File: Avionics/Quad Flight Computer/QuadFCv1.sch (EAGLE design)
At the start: 122 parts, among them J2 1050270001, Q1 DMP2035U, Q2 DMP2035U, Q3 DMP2035U, SW1 PTS635VL31-VERT, U1 TM4C123GH6PZ, U10 LTC4412, U11 AP7215-33YG-13, U2 74LVC4245APW, U3 ATMEGA32U2-MU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

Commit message: Added some connectors
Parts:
- added JP1, JP2: M101X10-SMT-0.05, QuadFCv1:M101X10-SMT-0.05
- added JP3, JP4: M12, QuadFCv1:M12
- added R57: 0, QuadFCv1:RESISTOR0402-RES
- added R58, R59: 10K, QuadFCv1:RESISTOR0402-RES
- added U4: MCP6L91T-E/OT, QuadFCv1:MCP6L91T-E/OT
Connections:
- removed net EXT_I2C_SCL: I2C.3
- removed net EXT_I2C_SDA: I2C.2
- removed net FC_AIN0: U1PORTE.PE3/AIN0
- removed net FC_AIN1: U1PORTE.PE2/AIN1
- removed net FC_AIN20: U1PORTE.PE7/AIN20/CAN1TX/U1RI
- removed net FC_AIN21: U1PORTE.PE6/AIN21/CAN1RX
- removed net FC_AIN4: U1PORTD.PD7/AIN4/M0FAULT1/NMI/PHB0/U2TX/WT5CCP1
- removed net FC_AIN5: U1PORTD.PD6/AIN5/M0FAULT0/PHA0/U2RX/WT5CCP0
- removed net FC_PA6: U1PORTA.PA6/I2C1SCL/M1PWM2
- removed net FC_PA7: U1PORTA.PA7/I2C1SDA/M1PWM3
- removed net FC_PD5: U1PORTD.PD5/AIN6/U6TX/WT4CCP1
- removed net FC_PF4: U1PORTF.PF4/IDX0/M0FAULT2/M1FAULT0/T2CCP0/TRD3/U1DTR/USB0EPEN
- removed net FC_PF5: U1PORTF.PF5/M0FAULT3/T2CCP1/USB0PFLT
- removed net FC_PF6: U1PORTF.PF6/I2C2SCL/T3CCP0
- removed net FC_PF7: U1PORTF.PF7/I2C2SDA/M1FAULT0/T3CCP1
- removed net FC_PJ2: U1PORTJ.PJ2/IDX0/T2CCP0/U5RX
- removed net FC_U0RX: U1PORTA.PA0/CAN1RX/U0RX
- removed net FC_U0TX: U1PORTA.PA1/CAN1TX/U0TX
- removed net FC_U1RX: U1PORTC.PC4/C1-/IDX1/M0PWM6/U1RTS/U1RX/U4RX/WT0CCP0
- removed net FC_U1TX: U1PORTC.PC5/C1+/M0PWM7/PHA1/U1CTS/U1TX/U4TX/WT0CCP1
- removed net FC_U3RX: U1PORTC.PC6/C0+/PHB1/U3RX/USB0EPEN/WT1CCP0
- removed net FC_U3TX: U1PORTC.PC7/C0-/U3TX/USB0PFLT/WT1CCP1
- removed net FC_U7RX: U1PORTE.PE0/AIN3/U7RX
- removed net FC_U7TX: U1PORTE.PE1/AIN2/U7TX
- removed net FC_USB0VBUS: U1PORTB.PB1/T2CCP1/U1TX/USB0VBUS
- removed net PPM_VBUS: U3.UVCC
- removed net RADIO_UART_RX: RADIO1.3
- removed net RADIO_UART_TX: RADIO1.2
- new net BUZZER_PWM: U1PORTA.PA7/I2C1SDA/M1PWM3, U4.+IN
- new net N$40: R57.1, U4.OUT
- new net N$43: R58.1, R59.2, U4.-IN
- new net RADIO_RX: RADIO1.3, U1PORTE.PE0/AIN3/U7RX
- new net RADIO_TX: RADIO1.2, U1PORTE.PE1/AIN2/U7TX
- new net VUSB_F: F1.1, Q1.D, Q3.S, U1PORTB.PB1/T2CCP1/U1TX/USB0VBUS, U3.UVCC
- net 3.3V: now also R58.2
- net 5V: now also U4.V+
- net FC_IMU_INT: now also U1PORTF.PF7/I2C2SDA/M1FAULT0/T3CCP1
- net FC_MAG_DRDY_L: now also U1PORTA.PA6/I2C1SCL/M1PWM2
- net FC_MEM_SEL: now also U1PORTJ.PJ2/IDX0/T2CCP0/U5RX
- net FC_PPM_IN: now also U1PORTC.PC7/C0-/U3TX/USB0PFLT/WT1CCP1
- net FC_PPM_STATUS0: now also U1PORTF.PF6/I2C2SCL/T3CCP0
- net FC_PPM_STATUS1: now also U1PORTF.PF5/M0FAULT3/T2CCP1/USB0PFLT
- net FC_SD_PRESENT: now also U1PORTD.PD5/AIN6/U6TX/WT4CCP1
- net FC_SENSE_SCL: now also I2C.3
- net FC_SENSE_SDA: now also I2C.2
- net FC_USB_STATUS: now also U1PORTF.PF4/IDX0/M0FAULT2/M1FAULT0/T2CCP0/TRD3/U1DTR/USB0EPEN
- net GND: now also BZR.2, R59.1, U4.V-
- net GPS_RX: now also U1PORTC.PC4/C1-/IDX1/M0PWM6/U1RTS/U1RX/U4RX/WT0CCP0
- net GPS_TX: now also U1PORTC.PC5/C1+/M0PWM7/PHA1/U1CTS/U1TX/U4TX/WT0CCP1
- net ISENSE1: now also U1PORTE.PE7/AIN20/CAN1TX/U1RI
- net ISENSE2: now also U1PORTE.PE6/AIN21/CAN1RX
- net ISENSE3: now also U1PORTE.PE3/AIN0
- net ISENSE4: now also U1PORTD.PD7/AIN4/M0FAULT1/NMI/PHB0/U2TX/WT5CCP1
- net ISENSE5V: now also U1PORTD.PD6/AIN5/M0FAULT0/PHA0/U2RX/WT5CCP0
- net N$42: now also BZR.1, R57.2; no longer F1.1, Q1.D, Q3.S
- net PPM_RX: now also U1PORTA.PA0/CAN1RX/U0RX
- net PPM_TX: now also U1PORTA.PA1/CAN1TX/U0TX
- net USB_EPEN: now also U1PORTC.PC6/C0+/PHB1/U3RX/USB0EPEN/WT1CCP0
- net VBATTSENSE: now also U1PORTE.PE2/AIN1

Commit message: Finished pinout for shield headers
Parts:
- added R60: 100k, QuadFCv1:RESISTOR0402-RES
- JP2: value M101X10-SMT-0.05 -> M12; device QuadFCv1:M101X10-SMT-0.05 -> QuadFCv1:M12
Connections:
- net 3.3V: now also JP3.2
- net 5V: now also JP3.1
- net 5VBATT: now also R60.2
- net BUZZER_PWM: now also JP1.5
- net FC_IMU_MISO: now also JP2.2
- net FC_IMU_MOSI: now also JP2.3
- net FC_IMU_SCLK: now also JP2.1
- net FC_JTAG_TCK: now also JP4.5
- net FC_JTAG_TDI: now also JP4.7
- net FC_JTAG_TDO: now also JP4.8
- net FC_JTAG_TMS: now also JP4.6
- net FC_MEM_CLK: now also JP3.4
- net FC_MEM_MISO: now also JP3.5
- net FC_MEM_MOSI: now also JP3.3
- net FC_PB2: now also JP4.12
- net FC_PB3: now also JP4.11
- net FC_PB4: now also JP4.1
- net FC_PB5: now also JP4.2
- net FC_PD0: now also JP3.9
- net FC_PD1: now also JP3.8
- net FC_PD2: now also JP3.7
- net FC_PD3: now also JP3.6
- net FC_PD4: now also JP3.10
- net FC_PE4: now also JP3.12
- net FC_PE5: now also JP3.11
- net FC_PF0: now also JP2.4
- net FC_PF1: now also JP2.5
- net FC_PF2: now also JP2.6
- net FC_PF3: now also JP2.7
- net FC_PG2: now also JP2.10
- net FC_PG3: now also JP2.9
- net FC_PG4: now also JP4.10
- net FC_PG5: now also JP4.9
- net FC_PG6: now also JP4.4
- net FC_PG7: now also JP4.3
- net FC_RESET_L: now also JP2.8
- net FC_SENSE_SCL: now also JP2.11
- net FC_SENSE_SDA: now also JP2.12
- net GND: now also JP1.1, JP1.2
- net GPS_RX: now also JP1.6
- net GPS_TX: now also JP1.7
- net PPM_RX: now also JP1.8
- net PPM_TX: now also JP1.9
- net RADIO_RX: now also JP1.3
- net RADIO_TX: now also JP1.4
- net USB_EPEN: now also R60.1
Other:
- moved on the sheet: JP1, JP3, JP4

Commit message: Lots more routing done
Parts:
- removed R3, R5: 22-DNP, QuadFCv1:RESISTOR0402-RES
- removed R36: 1k, QuadFCv1:RESISTOR0402-RES
- removed R8, R9: DNP, QuadFCv1:RESISTOR0603-RES
- C12, C9: value 1uF -> 1.8uF
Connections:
- removed net FC_USB_STATUS: R36.1, U1PORTF.PF4/IDX0/M0FAULT2/M1FAULT0/T2CCP0/TRD3/U1DTR/USB0EPEN
- removed net N$28: R3.2, R7.2, U12.D-
- removed net PPM_USBDM: R3.1, U3.D-
- removed net PPM_USBDP: R5.1, U3.D+
- removed net PPM_USB_STATUS: R36.2, U3.(AIN2/PCINT11)PC2
- new net FC_PF4: JP2.8, U1PORTF.PF4/IDX0/M0FAULT2/M1FAULT0/T2CCP0/TRD3/U1DTR/USB0EPEN
- new net N$49: R7.2, U12.D-
- net 5V: now also U3.UVCC; no longer R8.2
- net 5VBATT: no longer R9.2
- net FC_PD4: now also JP3.12; no longer JP3.10
- net FC_PE4: now also JP3.10; no longer JP3.12
- net FC_RESET_L: now also JP1.10; no longer JP2.8
- net N$23: no longer R9.1
- net N$26: no longer R8.1
- net N$29: no longer R5.2
- net VUSB_F: no longer U3.UVCC

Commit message: More routing
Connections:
- net FC_IMU_MOSI: now also JP2.1; no longer JP2.3
- net FC_IMU_SCLK: now also JP2.3; no longer JP2.1
- net FC_PF0: now also JP2.5; no longer JP2.4
- net FC_PF1: now also JP2.6; no longer JP2.5
- net FC_PF2: now also JP2.7; no longer JP2.6
- net FC_PF3: now also JP2.8; no longer JP2.7
- net FC_PF4: now also JP2.4; no longer JP2.8
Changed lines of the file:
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@@
 <net name="FC_IMU_SCLK" class="0">
 <segment>
-<pinref part="JP2" gate="G$1" pin="1"/>
-<wire x1="-35.56" y1="7.62" x2="-22.86" y2="7.62" width="0.1524" layer="91"/>
-<label x="-27.94" y="7.62" size="1.778" layer="95"/>
+<pinref part="JP2" gate="G$1" pin="3"/>
+<wire x1="-35.56" y1="12.7" x2="-22.86" y2="12.7" width="0.1524" layer="91"/>
+<label x="-27.94" y="12.7" size="1.778" layer="95"/>
 </segment>
 </net>
@@
 </segment>
 </net>
-<net name="FC_IMU_MOSI" class="0">
-<segment>
-<pinref part="JP2" gate="G$1" pin="3"/>
-<wire x1="-35.56" y1="12.7" x2="-22.86" y2="12.7" width="0.1524" layer="91"/>
-<label x="-27.94" y="12.7" size="1.778" layer="95"/>
-</segment>
-</net>
 <net name="FC_SENSE_SCL" class="0">
 <segment>
@@
 <net name="FC_PF1" class="0">
 <segment>
+<wire x1="-35.56" y1="20.32" x2="-22.86" y2="20.32" width="0.1524" layer="91"/>
+<label x="-27.94" y="20.32" size="1.778" layer="95"/>
+<pinref part="JP2" gate="G$1" pin="6"/>
+</segment>
+</net>
+<net name="FC_PF0" class="0">
+<segment>
+<wire x1="-22.86" y1="17.78" x2="-35.56" y2="17.78" width="0.1524" layer="91"/>
+<label x="-27.94" y="17.78" size="1.778" layer="95"/>
 <pinref part="JP2" gate="G$1" pin="5"/>
-<wire x1="-35.56" y1="17.78" x2="-22.86" y2="17.78" width="0.1524" layer="91"/>
-<label x="-27.94" y="17.78" size="1.778" layer="95"/>
-</segment>
-</net>
-<net name="FC_PF0" class="0">
-<segment>
-<pinref part="JP2" gate="G$1" pin="4"/>
-<wire x1="-22.86" y1="15.24" x2="-35.56" y2="15.24" width="0.1524" layer="91"/>
-<label x="-27.94" y="15.24" size="1.778" layer="95"/>
 </segment>
 </net>
@@
 <net name="FC_PF2" class="0">
 <segment>
-<pinref part="JP2" gate="G$1" pin="6"/>
-<wire x1="-22.86" y1="20.32" x2="-35.56" y2="20.32" width="0.1524" layer="91"/>
-<label x="-27.94" y="20.32" size="1.778" layer="95"/>
+<wire x1="-22.86" y1="22.86" x2="-35.56" y2="22.86" width="0.1524" layer="91"/>
+<label x="-27.94" y="22.86" size="1.778" layer="95"/>
+<pinref part="JP2" gate="G$1" pin="7"/>
 </segment>
 </net>
 <net name="FC_PF3" class="0">
 <segment>
-<pinref part="JP2" gate="G$1" pin="7"/>
-<wire x1="-35.56" y1="22.86" x2="-22.86" y2="22.86" width="0.1524" layer="91"/>
-<label x="-27.94" y="22.86" size="1.778" layer="95"/>
+<wire x1="-35.56" y1="25.4" x2="-22.86" y2="25.4" width="0.1524" layer="91"/>
+<label x="-27.94" y="25.4" size="1.778" layer="95"/>
+<pinref part="JP2" gate="G$1" pin="8"/>
 </segment>
 </net>
@@
 <net name="FC_PF4" class="0">
 <segment>
-<pinref part="JP2" gate="G$1" pin="8"/>
-<wire x1="-35.56" y1="25.4" x2="-22.86" y2="25.4" width="0.1524" layer="91"/>
-<label x="-27.94" y="25.4" size="1.778" layer="95"/>
+<pinref part="JP2" gate="G$1" pin="4"/>
+<wire x1="-22.86" y1="15.24" x2="-35.56" y2="15.24" width="0.1524" layer="91"/>
+<label x="-27.94" y="15.24" size="1.778" layer="95"/>
 </segment>
 </net>
@@
 </segment>
 </net>
+<net name="FC_IMU_MOSI" class="0">
+<segment>
+<pinref part="JP2" gate="G$1" pin="1"/>
+<wire x1="-35.56" y1="7.62" x2="-22.86" y2="7.62" width="0.1524" layer="91"/>
+<label x="-27.94" y="7.62" size="1.778" layer="95"/>
+</segment>
+</net>

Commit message: Only 4 wires left. Sooo close
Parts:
- removed LED1: RED, QuadFCv1:LED0603
- removed LED2: ORANGE, QuadFCv1:LED0603
- removed R33, R34: 1k, QuadFCv1:RESISTOR0402-RES
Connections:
- removed net N$30: LED1.A, R33.2
- removed net N$31: LED2.A, R34.2
- net 5V: no longer R33.1, R34.1
- net FC_IMU_INT: now also U1PORTC.PC7/C0-/U3TX/USB0PFLT/WT1CCP1; no longer U1PORTF.PF7/I2C2SDA/M1FAULT0/T3CCP1
- net FC_PPM_IN: now also U1PORTF.PF7/I2C2SDA/M1FAULT0/T3CCP1; no longer U1PORTC.PC7/C0-/U3TX/USB0PFLT/WT1CCP1
- net PPM_RX: no longer JP1.8
- net PPM_TX: no longer JP1.9
- net RXLED: no longer LED2.C
- net TXLED: no longer LED1.C
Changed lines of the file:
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@@
 <part name="C15" library="QuadFCv1" deviceset="CAP" device="0402-CAP" value=".1uF"/>
 <part name="C16" library="QuadFCv1" deviceset="CAP" device="0402-CAP" value="1uF"/>
-<part name="LED1" library="QuadFCv1" deviceset="LED" device="0603" value="RED"/>
-<part name="LED2" library="QuadFCv1" deviceset="LED" device="0603" value="ORANGE"/>
-<part name="R33" library="QuadFCv1" deviceset="RESISTOR" device="0402-RES" value="1k"/>
-<part name="R34" library="QuadFCv1" deviceset="RESISTOR" device="0402-RES" value="1k"/>
 <part name="X1" library="QuadFCv1" deviceset="87758-0216" device="" value="HWB"/>
 <part name="PPM" library="QuadFCv1" deviceset="TESTPAD_TPSQ" device="TP10SQ"/>
@@
 </segment>
 </net>
-<net name="FC_IMU_INT" class="0">
-<segment>
-<pinref part="U1" gate="PORTF" pin="PF7/I2C2SDA/M1FAULT0/T3CCP1"/>
-<wire x1="-12.7" y1="-5.08" x2="17.78" y2="-5.08" width="0.1524" layer="91"/>
-<label x="-12.7" y="-5.08" size="1.778" layer="95"/>
-</segment>
-</net>
 <net name="FC_SENSE_SCL" class="0">
 <segment>
@@
 <net name="FC_PPM_IN" class="0">
 <segment>
+<pinref part="U1" gate="PORTF" pin="PF7/I2C2SDA/M1FAULT0/T3CCP1"/>
+<wire x1="-12.7" y1="-5.08" x2="17.78" y2="-5.08" width="0.1524" layer="91"/>
+<label x="-12.7" y="-5.08" size="1.778" layer="95"/>
+</segment>
+</net>
+<net name="FC_IMU_INT" class="0">
+<segment>
 <pinref part="U1" gate="PORTC" pin="PC7/C0-/U3TX/USB0PFLT/WT1CCP1"/>
 <wire x1="-167.64" y1="-63.5" x2="-147.32" y2="-63.5" width="0.1524" layer="91"/>
@@
 <attribute name="VALUE" x="-36.576" y="-25.019" size="1.778" layer="96"/>
 </instance>
-<instance part="LED1" gate="G$1" x="73.66" y="-43.18" rot="R270"/>
-<instance part="LED2" gate="G$1" x="73.66" y="-53.34" rot="R270"/>
-<instance part="R33" gate="G$1" x="81.28" y="-43.18" rot="R180"/>
-<instance part="R34" gate="G$1" x="81.28" y="-53.34" rot="R180"/>
 <instance part="X1" gate="-1" x="111.76" y="25.4"/>
 <instance part="X1" gate="-2" x="111.76" y="20.32"/>
@@
 <pinref part="U3" gate="G$1" pin="(INT5/AIN3)PD4"/>
 </segment>
-<segment>
-<wire x1="68.58" y1="-53.34" x2="58.42" y2="-53.34" width="0.1524" layer="91"/>
-<label x="58.42" y="-53.34" size="1.778" layer="95"/>
-<pinref part="LED2" gate="G$1" pin="C"/>
-</segment>
 </net>
 <net name="TXLED" class="0">
@@
 <pinref part="U3" gate="G$1" pin="(XCK/AIN4/PCINT12)PD5"/>
 </segment>
-<segment>
-<wire x1="68.58" y1="-43.18" x2="58.42" y2="-43.18" width="0.1524" layer="91"/>
-<label x="58.42" y="-43.18" size="1.778" layer="95"/>
-<pinref part="LED1" gate="G$1" pin="C"/>
-</segment>
 </net>
 <net name="XT1R" class="0">
@@
 </segment>
 </net>
-<net name="N$30" class="0">
-<segment>
-<pinref part="LED1" gate="G$1" pin="A"/>
-<pinref part="R33" gate="G$1" pin="2"/>
-</segment>
-</net>
-<net name="N$31" class="0">
-<segment>
-<pinref part="LED2" gate="G$1" pin="A"/>
-<pinref part="R34" gate="G$1" pin="2"/>
-</segment>
-</net>
 <net name="PPM_PD1" class="0">
 <segment>
@@
 </segment>
 <segment>
-<wire x1="86.36" y1="-43.18" x2="93.98" y2="-43.18" width="0.1524" layer="91"/>
 <wire x1="93.98" y1="-53.34" x2="93.98" y2="-43.18" width="0.1524" layer="91"/>
-<wire x1="86.36" y1="-53.34" x2="93.98" y2="-53.34" width="0.1524" layer="91"/>
-<pinref part="R33" gate="G$1" pin="1"/>
-<pinref part="R34" gate="G$1" pin="1"/>
 <pinref part="R35" gate="G$1" pin="1"/>
 <wire x1="86.36" y1="-63.5" x2="93.98" y2="-63.5" width="0.1524" layer="91"/>
 <wire x1="93.98" y1="-63.5" x2="93.98" y2="-53.34" width="0.1524" layer="91"/>
-<junction x="93.98" y="-53.34"/>
 <pinref part="SUPPLY12" gate="G$1" pin="5V"/>
-<junction x="93.98" y="-43.18"/>
 </segment>
 <segment>
@@
 </segment>
 </net>
-<net name="PPM_RX" class="0">
-<segment>
-<pinref part="JP1" gate="G$1" pin="8"/>
-<wire x1="-22.86" y1="-12.7" x2="-35.56" y2="-12.7" width="0.1524" layer="91"/>
-<label x="-30.48" y="-12.7" size="1.778" layer="95"/>
-</segment>
-</net>
-<net name="PPM_TX" class="0">
-<segment>
-<pinref part="JP1" gate="G$1" pin="9"/>
-<wire x1="-35.56" y1="-10.16" x2="-22.86" y2="-10.16" width="0.1524" layer="91"/>
-<label x="-30.48" y="-10.16" size="1.778" layer="95"/>
-</segment>
-</net>

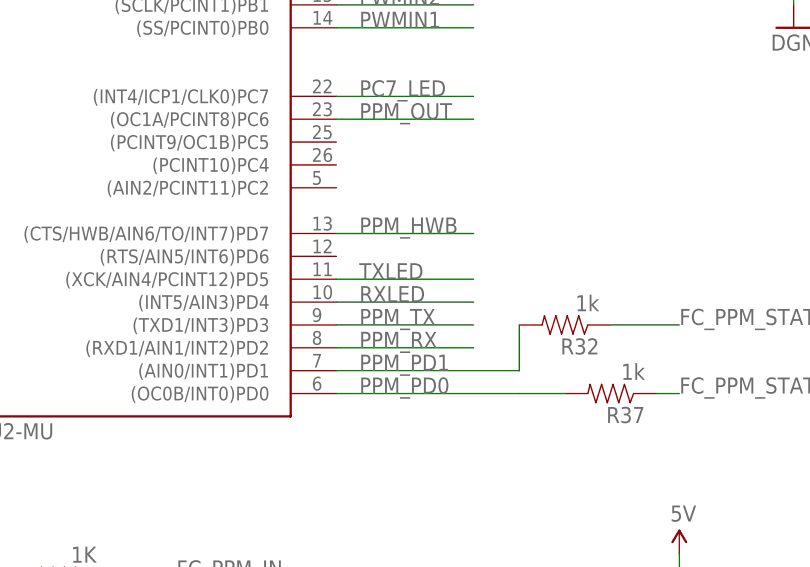
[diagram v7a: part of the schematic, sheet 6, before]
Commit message: Tracked down the last few airwires
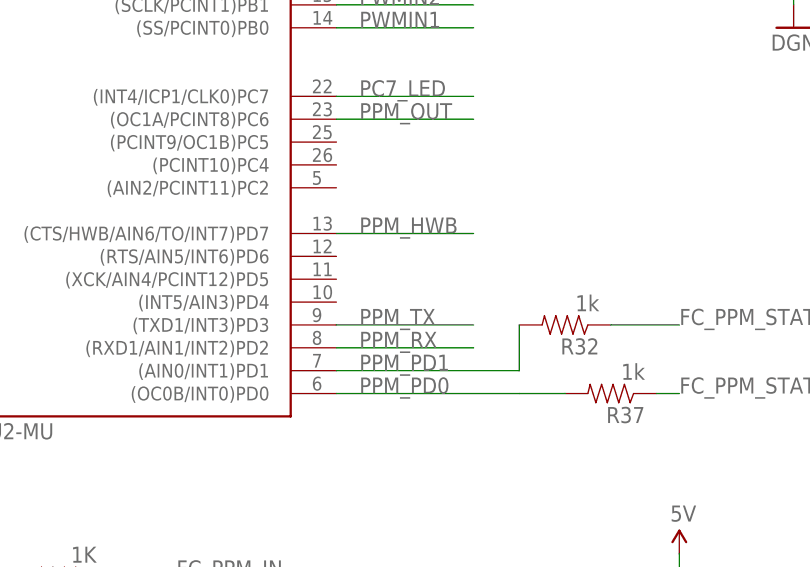
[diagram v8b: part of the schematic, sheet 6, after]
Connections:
- removed net RXLED: U3.(INT5/AIN3)PD4
- removed net TXLED: U3.(XCK/AIN4/PCINT12)PD5
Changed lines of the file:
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@@
-</segment>
-</net>
-<net name="RXLED" class="0">
-<segment>
-<wire x1="71.12" y1="-15.24" x2="55.88" y2="-15.24" width="0.1524" layer="91"/>
-<label x="58.42" y="-15.24" size="1.778" layer="95"/>
-<pinref part="U3" gate="G$1" pin="(INT5/AIN3)PD4"/>
-</segment>
-</net>
-<net name="TXLED" class="0">
-<segment>
-<wire x1="71.12" y1="-12.7" x2="55.88" y2="-12.7" width="0.1524" layer="91"/>
-<label x="58.42" y="-12.7" size="1.778" layer="95"/>
-<pinref part="U3" gate="G$1" pin="(XCK/AIN4/PCINT12)PD5"/>
 </segment>
 </net>
